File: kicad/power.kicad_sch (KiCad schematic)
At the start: 72 parts, among them J1 Bus_PCI_Express_x1, J2 Conn_01x02_Pin, J6 USB_C_Receptacle_USB2.0_16P, Q1 AO3400A, Q2 AO3400A, U1 MP2672GD-0000-Z, U2 MP2236CGJ-P, U3 MP2236CGJ-P, U4 MR30-M

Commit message: Update files for KiCad 9.0 and general Schematic updates
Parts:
- removed D1, D2: LED, LED_SMD:LED_0603_1608Metric, symbol Device:LED
- removed J1: Bus_PCI_Express_x1, Connector_PCBEdge:BUS_PCIexpress_x1, symbol Connector:Bus_PCI_Express_x1
- removed J2: Conn_01x02_Pin, Connector_PinHeader_2.54mm:PinHeader_1x02_P2.54mm_Vertical, symbol Connector:Conn_01x02_Pin
- removed R1, R2: 1k, Resistor_SMD:R_0402_1005Metric, symbol Device:R
- removed TP3: TestPoint, Connector_PinHeader_2.54mm:PinHeader_1x01_P2.54mm_Vertical, symbol Connector:TestPoint
- added C27, C28: 15p, Capacitor_SMD:C_0402_1005Metric, symbol Device:C
- added C29, C30, C32, C34, C35, C36, C38, C40, C41, C42, C43, C44, C45: 100n, Capacitor_SMD:C_0402_1005Metric, symbol Device:C
- added C31, C33: 22p, Capacitor_SMD:C_0402_1005Metric, symbol Device:C
- added C37, C39: 1u, Capacitor_SMD:C_0402_1005Metric, symbol Device:C
- added D5: LED, LED_SMD:LED_0603_1608Metric, symbol Device:LED
- added J4: Bus_PCI_Express_x1, Connector_PCBEdge:BUS_PCIexpress_x1, symbol Connector:Bus_PCI_Express_x1
- added J5: Conn_01x02_Pin, Connector_PinHeader_2.54mm:PinHeader_1x02_P2.54mm_Vertical, symbol Connector:Conn_01x02_Pin
- added J7: Conn_01x03, Connector_PinHeader_2.54mm:PinHeader_1x03_P2.54mm_Vertical, symbol Connector_Generic:Conn_01x02
- added R25, R26: 1k, Resistor_SMD:R_0402_1005Metric, symbol Device:R
- added R29: 10k, Resistor_SMD:R_0402_1005Metric, symbol Device:R
- added R30: 1 k, Resistor_SMD:R_0603_1608Metric, symbol Device:R
- added R31, R32: 27, Resistor_SMD:R_0402_1005Metric, symbol Device:R
- added S2: TS-1187A-B-A-B, GPSLIB:SW_TS-1187A-B-A-B, symbol TS-1187A-B-A-B:TS-1187A-B-A-B
- added U5: W25Q128JVP, Package_SON:WSON-8-1EP_6x5mm_P1.27mm_EP3.4x4.3mm, symbol Memory_Flash:W25Q128JVP
- added U6: MCP25625T-E/ML, GPSLIB:QFN28_6X6MC_MCH, symbol MCP25625:MCP25625T-E_ML
- added U7: RP2040, Package_DFN_QFN:QFN-56-1EP_7x7mm_P0.4mm_EP3.2x3.2mm, symbol MCU_RaspberryPi:RP2040
- added X1: ABM8-272-T3, GPSLIB:ABM8-272-T3_ABR, symbol crystal:ABM8-272-T3
- added Y1: X322516MLB4SI, GPSLIB:OSC_X322516MLB4SI, symbol X322516MLB4SI:X322516MLB4SI
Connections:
- net +3.3V: now also C29.1, C30.1, C32.1, C38.1, C39.1, C40.1, C41.1, C42.1, C43.1, C44.1, C45.1, D5.2 (A), J4.A10 (+3.3V), J4.A11 (~{PERST}), J4.A9 (+3.3V), J4.B10 (3.3Vaux), J4.B11 (~{WAKE}), J4.B9 (JTAG1), R29.1, U5.8 (VCC), U6.11 (VIO), U6.3 (VDD), U7.1 (IOVDD), U7.10 (IOVDD), U7.22 (IOVDD), U7.33 (IOVDD), U7.42 (IOVDD), U7.43 (ADC_AVDD), U7.44 (VREG_IN), U7.48 (USB_VDD), U7.49 (IOVDD)
- net +5V: now also C34.1, J4.A12 (GND), J4.A13 (REFCLK+), J4.A14 (REFCLK-), J4.B12 (RSVD), J4.B13 (GND), J4.B14 (PETp0), U6.19 (VDDA)
- net CANN: now also J4.A3 (+12V), U6.12 (CANL)
- net CANP: now also J4.A1 (~{PRSNT1}), U6.13 (CANH)
- net GND: now also C27.2, C28.2, C29.2, C30.2, C31.2, C32.2, C33.2, C34.2, C35.2, C36.2, C37.2, C38.2, C39.2, C40.2, C41.2, C42.2, C43.2, C44.2, C45.2, J4.A4 (GND), J4.A5 (JTAG2), J4.A6 (JTAG3), J4.A7 (JTAG4), J4.B1 (+12V), J4.B2 (+12V), J4.B3 (+12V), J4.B4 (GND), J4.B5 (SMCLK), J4.B6 (SMDAT), J4.B7 (GND), J5.2 (Pin_2), J7.2 (Pin_2), R30.2, S2.A, S2.B, U5.4 (GND), U6.18 (VSS), U6.22 (GND), U6.29 (EPAD), U7.19 (TESTEN), U7.57 (GND), X1.2, X1.4, Y1.2, Y1.4
- new net: D5.1 (K), R30.1
- new net +1.1V: C35.1, C36.1, C37.1, U7.23 (DVDD), U7.45 (VREG_VOUT), U7.50 (DVDD)
- new net CANINT: U6.25 (*INT), U7.35 (GPIO23)
- new net CANRESET: R29.2, U6.2 (*RESET), U7.27 (GPIO16)
- new net CANSTBY: U6.15 (STBY), U7.38 (GPIO26_ADC0)
- new net CS: U6.1 (*CS), U7.28 (GPIO17)
- new net OSC1: C31.1, U6.21 (OSC1), Y1.1
- new net OSC2: C33.1, U6.20 (OSC2), Y1.3
- new net QSPI_SCLK: U5.6 (CLK), U7.52 (QSPI_SCLK)
- new net QSPI_SD0: U5.5 (DI(IO0)), U7.53 (QSPI_SD0)
- new net QSPI_SD1: U5.2 (DO(IO1)), U7.55 (QSPI_SD1)
- new net QSPI_SD2: U5.3 (IO2), U7.54 (QSPI_SD2)
- new net QSPI_SD3: U5.7 (IO3), U7.51 (QSPI_SD3)
- new net QSPI_SS: R25.1, U5.1 (~{CS}), U7.56 (QSPI_SS)
- new net RUN: S2.C, S2.D, U7.26 (RUN)
- new net SCK: U6.26 (SCK), U7.34 (GPIO22)
- new net SI: U6.27 (SI), U7.30 (GPIO19)
- new net SO: U6.28 (SO), U7.31 (GPIO20)
- new net SWCLK: J7.1 (Pin_1), U7.24 (SWCLK)
- new net SWD: J7.3 (Pin_3), U7.25 (SWD)
- new net U4_USB_D+: R31.2, U7.47 (USB_DP)
- new net U4_USB_D-: R32.2, U7.46 (USB_DM)
- new net USART4_RX: U7.41 (GPIO29_ADC3)
- new net USART4_TX: U7.40 (GPIO28_ADC2)
- new net USB_D+: R31.1
- new net USB_D-: R32.1
- new net XIN: C27.1, U7.20 (XIN), X1.1
- new net XOUT: R26.1, U7.21 (XOUT)
- new net XOUT_pre: C28.1, R26.2, X1.3
- new net rx: U6.10 (RXD), U6.5 (RXCAN)
- new net tx: U6.16 (TXD), U6.4 (TXCAN)
- new net ~{USB_BOOT_S}: J5.1 (Pin_1), R25.2
- no-connect marks 12 -> 45
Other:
- note added: "CAN"
- note added: "CAN Controller/Tranceiver"
- note added: "CAN Crystal"
- note added: "Close jumper to enable I2C pullups on bus"
- note added: "Flash"
- note added: "MCU"
- note added: "Make sure C210 is close to pin 44 of RP2040"
- note added: "Make sure C8 is close to pin 45 of RP2040"
- note added: "Make sure R3 and R4 are close to RP2040"
- note added: "Power Conections"
- note added: "Power Status LEDs"
- note added: "RP2040 Crystal"
- note added: "RP2040 MCU"
- note added: "Test Points"
- note added: "USB Boot shorting headders"
- moved on the sheet: C1, C10, C11, C12, C13, C14, C15, C16, C17, C18, C19, C2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

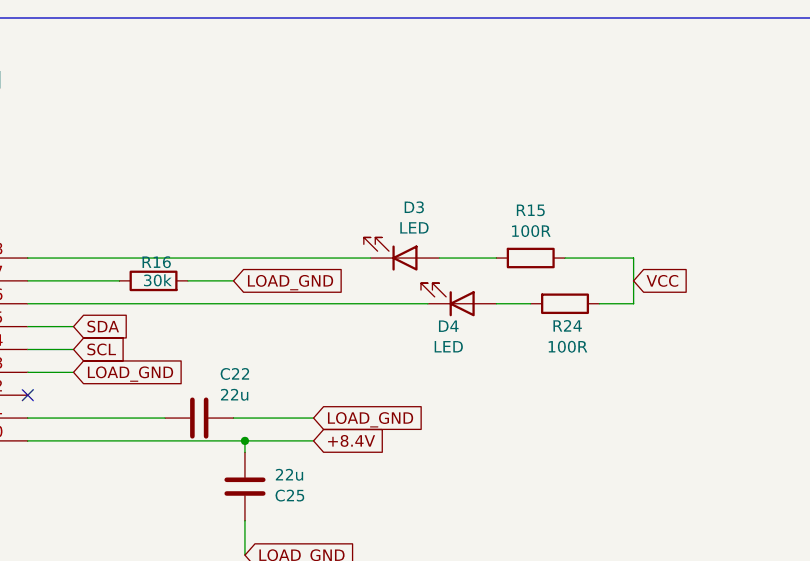
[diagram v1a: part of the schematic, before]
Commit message: Update footprints
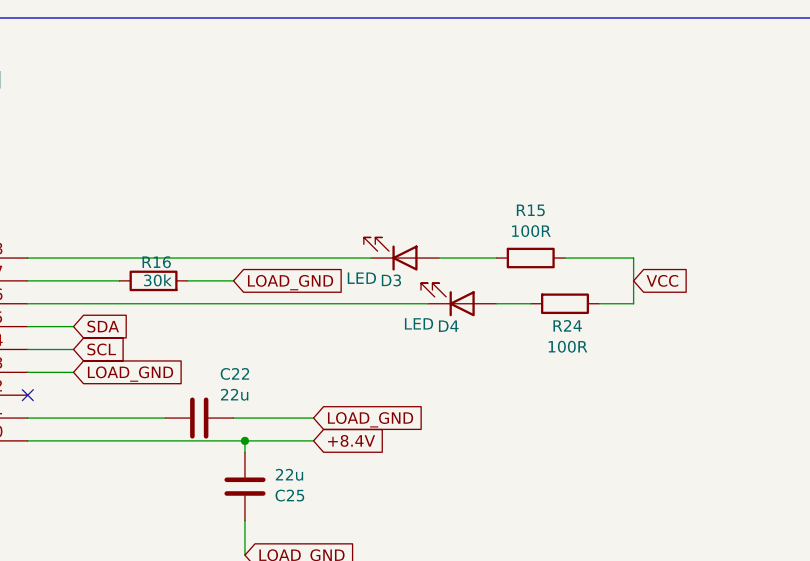
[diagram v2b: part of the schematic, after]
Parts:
- CR1: footprint SOT23-6L_STM -> Package_TO_SOT_SMD:SOT-23-6
- D3: footprint (none) -> LED_SMD:LED_0603_1608Metric; JLC Link (none) -> https://jlcpcb.com/partdetail/Hubei_KentoElec-KT0603R/C2286; LCSC Part # (none) -> C2286; info (none) -> Red LED; price (none) -> C$0.0075
- D4: footprint (none) -> LED_SMD:LED_0603_1608Metric; JLC Link (none) -> https://jlcpcb.com/partdetail/Hubei_KentoElec-KT0603B/C2288; LCSC Part # (none) -> C2288; info (none) -> Blue LED; price (none) -> C$0.0075
- L3: footprint IND-SMD_L7.0-W6.6 -> POWERLIB:IND-SMD_L7.0-W6.6
- Q1, Q2: footprint SOT-23-3_L2.9-W1.3-P1.90-LS2.4-BR -> Package_TO_SOT_SMD:SOT-23-3
- R22: footprint POWERLIB:NTC_R0402 -> Diode_SMD:D_0402_1005Metric

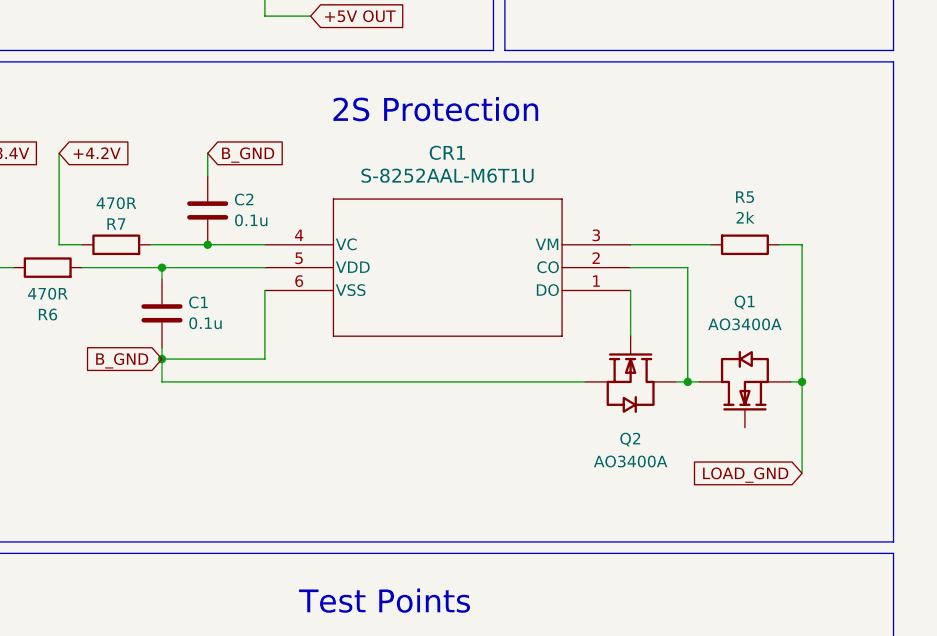
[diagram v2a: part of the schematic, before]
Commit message: Update FETs and Protection IC
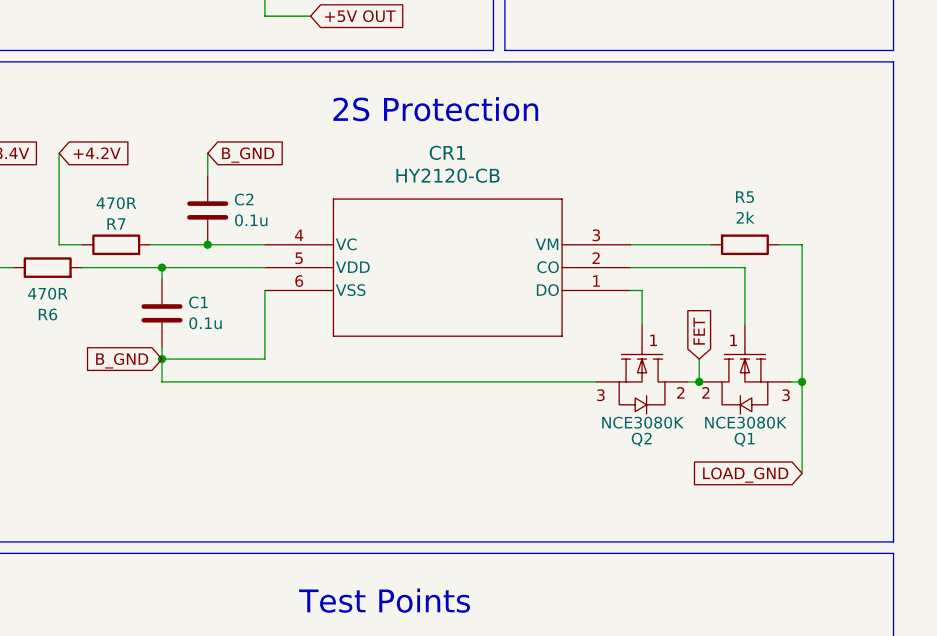
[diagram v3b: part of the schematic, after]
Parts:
- removed Q1, Q2: AO3400A, Package_TO_SOT_SMD:SOT-23-3, symbol powermodule:AO3400
- added Q1, Q2: NCE3080K, POWERLIB:TO-252-2_L6.6-W6.1-P4.57-LS9.9-TL-CW, symbol powermodule:NCE3080K
- CR1: value S-8252AAL-M6T1U -> HY2120-CB; Basic? (none) -> no; Comment (none) -> —; Current Draw (none) -> Not specified; Digikey Link (none) -> —; Info (none) -> Battery management IC; JLC Link (none) -> JLCPCB assembly availability (HY2120‑CB); LCSC Part # (none) -> C116509; Notes (none) -> Packaged in SOT‑23‑6, RoHS compliant, in stock (~85 units); Price (none) -> ≈ US $0.2066 each (for 5+) / as low as US $0.0896 in larger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
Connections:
- net B_GND: now also Q2.3 (S)
- net LOAD_GND: now also Q1.3 (S)
- net at CR1.2 (CO): now also Q1.1 (G)
- net at CR1.1 (DO): now also Q2.1 (G)
- new net FET: Q1.2 (D), Q2.2 (D)

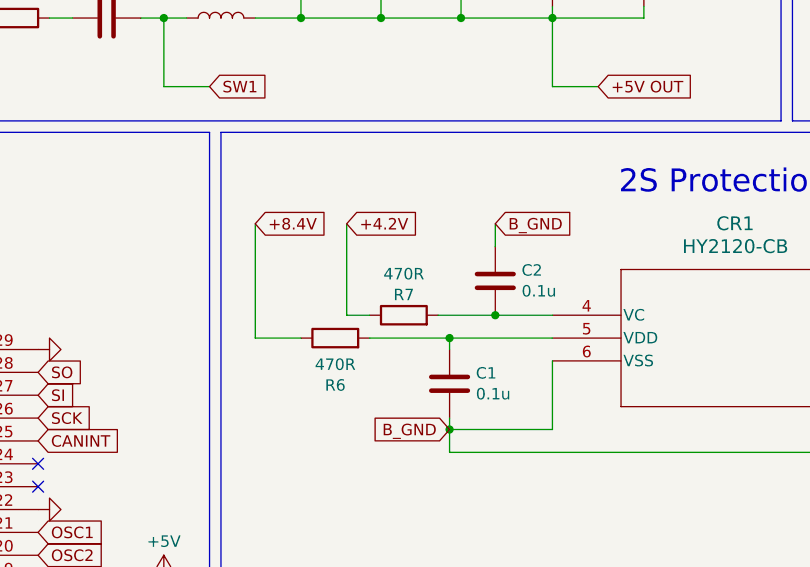
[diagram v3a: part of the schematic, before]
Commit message: Prototype BMS and Protection
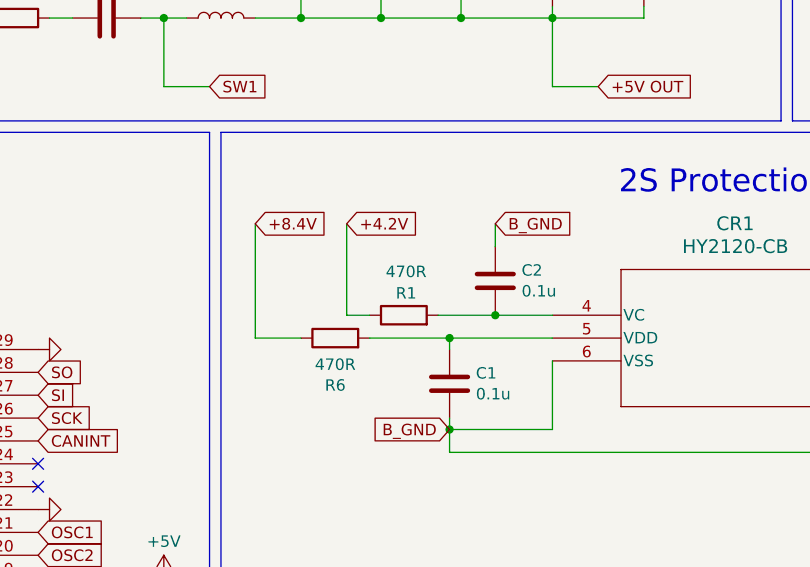
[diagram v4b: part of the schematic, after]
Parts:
- removed R7: 470R, Resistor_SMD:R_0402_1005Metric, symbol Device:R
- added R1: 470R, Resistor_SMD:R_1206_3216Metric, symbol Device:R
- C1, C15, C16, C2, C20, C23, C26: footprint Capacitor_SMD:C_0402_1005Metric -> Capacitor_SMD:C_0603_1608Metric
- C12, C13, C14, C17, C18, C19, C21, C22, C24: footprint Capacitor_SMD:C_0402_1005Metric -> Capacitor_SMD:C_0805_2012Metric
- C25: footprint Capacitor_SMD:C_0402_1005Metric -> Capacitor_SMD:C_1206_3216Metric
- R11, R17, R23, R6: footprint Resistor_SMD:R_0402_1005Metric -> Resistor_SMD:R_1206_3216Metric
- R12, R13, R14, R16, R18, R19, R20, R21, R5: footprint Resistor_SMD:R_0402_1005Metric -> Resistor_SMD:R_0603_1608Metric
- R15, R24: footprint Resistor_SMD:R_0402_1005Metric -> Resistor_SMD:R_0805_2012Metric
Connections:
- net +4.2V: now also R1.1
- net at C2.2, CR1.4 (VC): now also R1.2

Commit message: Fixing Zones
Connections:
- net L3P2: now reaches C26.1, L3.2, U1.2 (SW)
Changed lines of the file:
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@@
 	)
 	(junction
+		(at 229.87 38.1)
+		(diameter 0)
+		(color 0 0 0 0)
+	)
+	(junction
 		(at 208.28 217.17)
 		(diameter 0)
@@
 	(wire
 		(pts
+			(xy 229.87 38.1) (xy 231.14 38.1)
+		)
+		(stroke
+			(width 0)
+			(type default)
+		)
+	)
+	(wire
+		(pts
 			(xy 313.69 177.8) (xy 313.69 187.96)
 		)
@@
 	(wire
 		(pts
-			(xy 228.6 38.1) (xy 231.14 38.1)
+			(xy 228.6 38.1) (xy 229.87 38.1)
 		)
 		(stroke
@@
 	(wire
 		(pts
+			(xy 229.87 34.29) (xy 229.87 38.1)
+		)
+		(stroke
+			(width 0)
+			(type default)
+		)
+	)
+	(wire
+		(pts
 			(xy 93.98 71.12) (xy 95.25 71.12)
 		)
@@
 				(hide yes)
 			)
+		)
+	)
+	(global_label "L3P2"
+		(shape input)
+		(at 229.87 34.29 0)
+		(fields_autoplaced yes)
+		(effects
+			(font
+				(size 1.27 1.27)
+			)
+			(justify left)
+		)
+		(property "Intersheetrefs" "${INTERSHEET_REFS}"
+			(at 237.5723 34.29 0)
+			(effects
+				(font
+					(size 1.27 1.27)
+				)
+				(justify left)
+				(hide yes)
+			)
